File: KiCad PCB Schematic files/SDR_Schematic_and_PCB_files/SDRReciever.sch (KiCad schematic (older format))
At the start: 62 parts, among them J1 Conn_Coaxial, J10 I_0, J11 I_180, J12 Q_90, J13 Q_270, J16 5V, J17 4.3V, J2 AudioJack3, J3 FIL_I, J4 FIL_O, J5 CLK_1, J6 CLK_2, J7 CLK_0, Q1 PN2222A, Q2 BSS138, Q3 BSS138, U1 Si5351A-B-GT, U2 LM4562, U3 SN74CBT3253, Y1 ATS250

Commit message: Removed old KiCad version files, kept the latest and removed *02 appending
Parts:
- removed D1, D2: 1N914, Diode_THT:D_DO-35_SOD27_P7.62mm_Horizontal, symbol SDRReciever-rescue:1N914-Diode
- added J8: 3.3V, Connector_PinHeader_2.54mm:PinHeader_1x01_P2.54mm_Vertical, symbol SDRReciever-rescue:Conn_01x01-Connector_Generic-SDRReciever-rescue
- A1: symbol SDRReciever-rescue:Arduino_Nano_v3.x-MCU_Module -> SDRReciever-rescue:Arduino_Nano_v3.x-MCU_Module-SDRReciever-rescue
- C1, C3: footprint Capacitor_THT:C_Disc_D4.7mm_W2.5mm_P5.00mm -> Capacitor_SMD:C_0805_2012Metric; symbol SDRReciever-rescue:C-Device -> SDRReciever-rescue:C-Device-SDRReciever-rescue
- C10, C11, C12, C13, C4: footprint Capacitor_THT:C_Disc_D5.1mm_W3.2mm_P5.00mm -> Capacitor_SMD:C_0805_2012Metric; symbol SDRReciever-rescue:C-Device -> SDRReciever-rescue:C-Device-SDRReciever-rescue
- C14, C15, C16, C2, C5, C6, C7: footprint Capacitor_THT:C_Disc_D5.0mm_W2.5mm_P2.50mm -> Capacitor_SMD:C_0805_2012Metric; symbol SDRReciever-rescue:C-Device -> SDRReciever-rescue:C-Device-SDRReciever-rescue
- C9: footprint Capacitor_THT:CP_Radial_D5.0mm_P2.00mm -> Capacitor_SMD:C_0805_2012Metric; symbol SDRReciever-rescue:C-Device -> SDRReciever-rescue:C-Device-SDRReciever-rescue
- J1: symbol SDRReciever-rescue:Conn_Coaxial-Connector -> SDRReciever-rescue:Conn_Coaxial-Connector-SDRReciever-rescue
- J10, J11, J12, J13, J16, J17, J5, J6, J7: symbol SDRReciever-rescue:Conn_01x01-Connector_Generic -> SDRReciever-rescue:Conn_01x01-Connector_Generic-SDRReciever-rescue
- J2: symbol SDRReciever-rescue:AudioJack3-Connector -> SDRReciever-rescue:AudioJack3-Connector-SDRReciever-rescue
- J3: value FIL_I -> FIL_IN; symbol SDRReciever-rescue:Conn_01x01-Connector_Generic -> SDRReciever-rescue:Conn_01x01-Connector_Generic-SDRReciever-rescue
- J4: value FIL_O -> FIL_OUT; symbol SDRReciever-rescue:Conn_01x01-Connector_Generic -> SDRReciever-rescue:Conn_01x01-Connector_Generic-SDRReciever-rescue
- JP1, JP2, JP3, JP4: symbol SDRReciever-rescue:Jumper_NC_Small-Device -> SDRReciever-rescue:Jumper_NC_Small-Device-SDRReciever-rescue
- L1: footprint Inductor_THT:L_Toroid_Vertical_L13.0mm_W6.5mm_P5.60mm -> Inductor_THT:L_Toroid_Vertical_L10.0mm_W5.0mm_P5.08mm; symbol SDRReciever-rescue:L-Device -> SDRReciever-rescue:L-Device-SDRReciever-rescue
- L2: footprint Inductor_THT:L_Toroid_Vertical_L10.0mm_W5.0mm_P5.08mm -> Inductor_THT:L_Toroid_Vertical_L13.0mm_W6.5mm_P5.60mm; symbol SDRReciever-rescue:L-Device -> SDRReciever-rescue:L-Device-SDRReciever-rescue
- L3: symbol SDRReciever-rescue:L-Device -> SDRReciever-rescue:L-Device-SDRReciever-rescue
- Q1: symbol SDRReciever-rescue:PN2222A-Transistor_BJT -> SDRReciever-rescue:PN2222A-Transistor_BJT-SDRReciever-rescue
- R1, R10, R11, R12, R13, R14, R18, R19, R3, R4, R5: footprint Resistor_THT:R_Axial_DIN0207_L6.3mm_D2.5mm_P7.62mm_Horizontal -> Resistor_SMD:R_0805_2012Metric; symbol SDRReciever-rescue:R-Device -> SDRReciever-rescue:R-Device-SDRReciever-rescue
- R20, R21, R22, R23: symbol SDRReciever-rescue:R-Device -> SDRReciever-rescue:R-Device-SDRReciever-rescue
- R7, R8: footprint (none) -> Resistor_SMD:R_0805_2012Metric; symbol SDRReciever-rescue:R-Device -> SDRReciever-rescue:R-Device-SDRReciever-rescue
- U1: symbol SDRReciever-rescue:Si5351A-B-GT-Oscillator -> SDRReciever-rescue:Si5351A-B-GT-Oscillator-SDRReciever-rescue
- U2: symbol Amplifier_Operational:LM4562 -> SDRReciever-rescue:LM4562-Amplifier_Operational
- U3: symbol SDRReciever-rescue:SN74CBT3253-Analog_Switch -> SDRReciever-rescue:SN74CBT3253-Analog_Switch-SDRReciever-rescue
- Y1: value ATS250 -> CX3225SB; footprint Crystal:Crystal_HC49-U_Vertical -> Crystal:Crystal_SMD_Abracon_ABM8G-4Pin_3.2x2.5mm; symbol SDRReciever-rescue:Crystal-Device -> Device:Crystal_GND24; DigiKey (none) -> https://www.digikey.com/en/products/detail/kyocera-internat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
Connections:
- wire segments 183 -> 181
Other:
- note added: "CX3225SB\n25 MHz crystal"
- note added: "Full Scale Input \nSignal Level Typ: 1.0 Vrms\nInput R = 55kΩ?????"
- note added: "Optional\nbypass jumper"
- note added: "T37-6 Toroid:\n11.9 turns"
- note added: "T50-6 Toroid: \n14.3 turns"
- note removed: "Full Scale Input \nSignal Level Typ: 1.0 Vrms\nInput R = 55kΩ."
- note removed: "NOTE:\nDouble check values of C5-C8\n100nf?"
- note removed: "Note:\nCheck all footprints\nExchange some through hole components for surface mount"
- note removed: "T37-6 Toroid:\n-- turns"
- note removed: "T50-6 Toroid: \n-- turns"
- note removed: "The ATS250 is \na low-cost 25 \nMHz crystal\n\nCX3225\n25 MHz crystal"
- note removed: "Voltage Protection Diodes:\nThese will prevent too large of signals \nfrom coming through"
- moved on the sheet: Q3

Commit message: Revision 0.3 of schematic Added bypass cap Added DC blocking caps Removed redudant resitors Added custom footprints Updated BNC connector footprint Updated audo jack footprint, schematic symbol, connections, and 3D model Updated comments Removed old PCB Created new blank PCB
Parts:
- removed R7, R8: 1k, Resistor_SMD:R_0805_2012Metric, symbol SDRReciever-rescue:R-Device-SDRReciever-rescue
- added C16: 0.1u, Capacitor_SMD:C_0805_2012Metric, symbol SDRReciever-rescue:C-Device-SDRReciever-rescue
- added C17, C18: 10u, Capacitor_SMD:C_0805_2012Metric, symbol SDRReciever-rescue:C-Device-SDRReciever-rescue
- J1: footprint Connector_Coaxial:SMA_Molex_73251-1153_EdgeMount_Horizontal -> Connector_TE-Connectivity:BNC_Socket_TYCO-AMP_LargePads
- J14: renamed from J2; footprint Connector_Audio:Jack_3.5mm_Switronic_ST-005-G_horizontal -> Connector_Audio:35RAPC4BHN2; symbol SDRReciever-rescue:AudioJack3-Connector-SDRReciever-rescue -> 35RAPC4BHN2:35RAPC4BHN2; Soundcard Datasheet (none) -> https://static.qobuz.com/info/IMG/pdf/VT1620A.pdf
- renumbered C9 to C1, C14 to C10, C15 to C11, C16 to C12, C5 to C13, C6 to C14, C7 to C15, C1 to C3, C3 to C4, C11 to C5, C4 to C6, C10 to C7, C12 to C8, C13 to C9, J8 to J2, J16 to J4, J17 to J5, J4 to J6, J6 to J7, J7 to J8, J5 to J9, JP3 to JP2, JP2 to JP3, L2 to L1, L1 to L2, R20 to R1, R11 to R10, R12 to R11, R4 to R12, R3 to R14, R14 to R15, R1 to R2, R21 to R3, R22 to R4, R23 to R5, R18 to R6, R19 to R7, R5 to R8, R10 to R9, U3 to U2, U2 to U3
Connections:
- net +4.3V: now also C16.1
- net GND: now also C16.2
- net at C14.1, R14.1, U3.7: now also C18.2; no longer J14.R
- net at JP4.2: now also J14.1; no longer J14.S
- net at C11.1, R12.1, U3.1: now also C17.2; no longer J14.T
- new net: C17.1, J14.2
- new net: C18.1, J14.3
- no-connect marks 24 -> 26
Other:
- note added: "DC Blocking\nCapcitor"
- note added: "Full Scale Input \nSignal Level Typ: 1.0 Vrms\nSound Card Input R = 55kΩ"
- note removed: "Full Scale Input \nSignal Level Typ: 1.0 Vrms\nInput R = 55kΩ?????"
- moved on the sheet: JP4

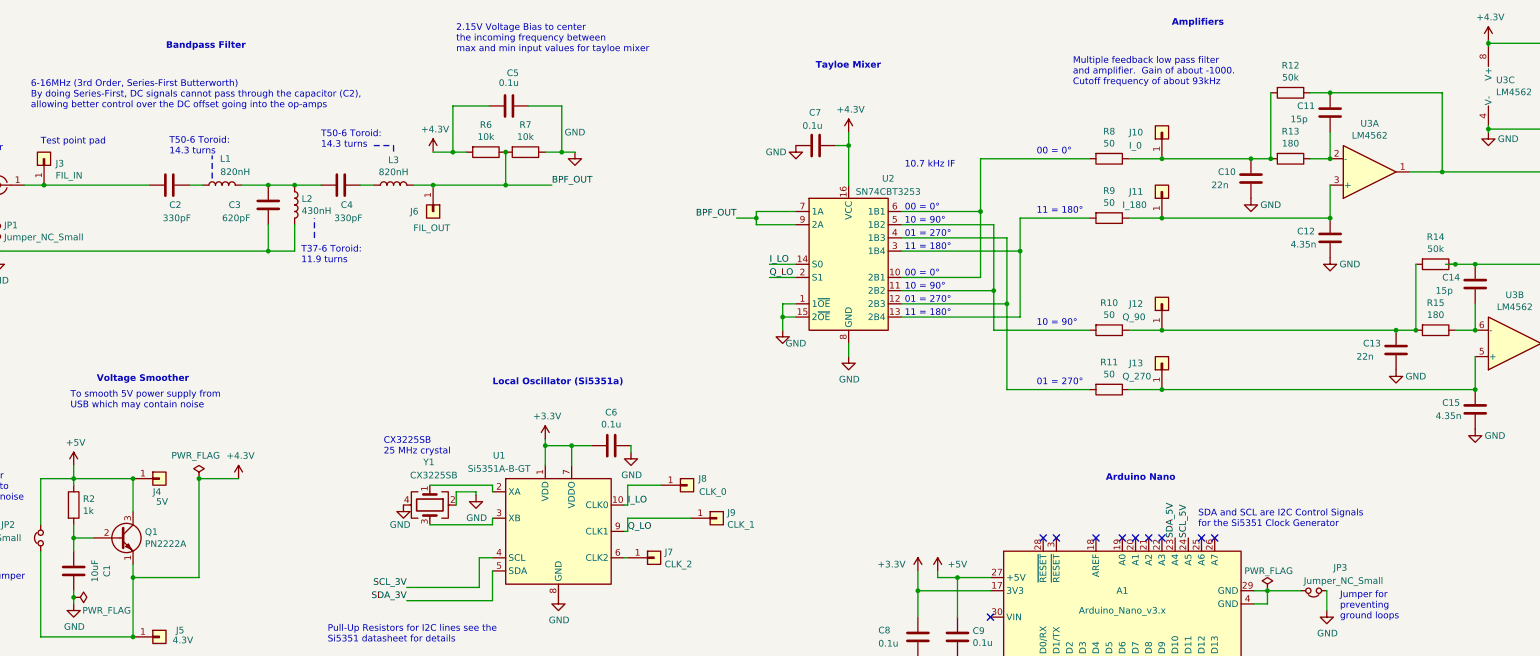
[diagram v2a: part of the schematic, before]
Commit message: Exchanged transistor for surface mount transistor Updated resistor values to standard values
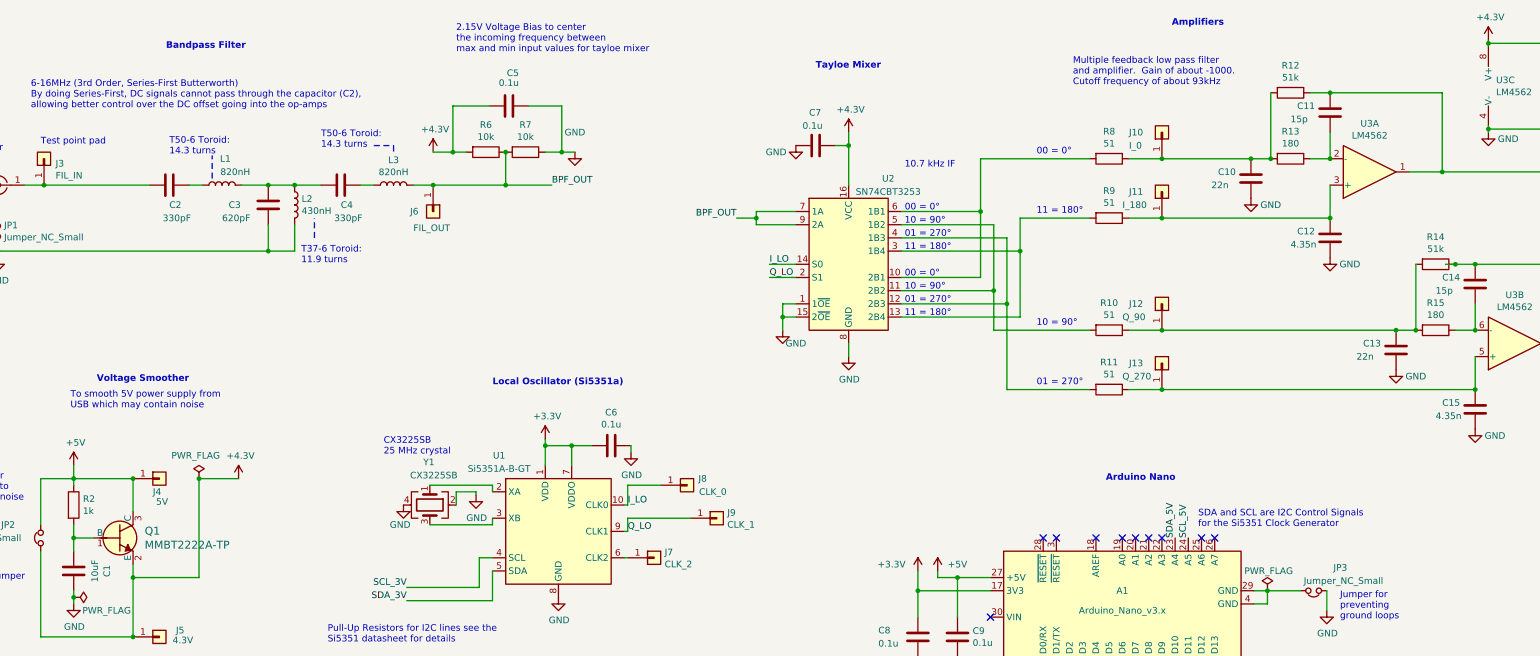
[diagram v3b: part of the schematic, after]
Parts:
- removed Q1: PN2222A, Package_TO_SOT_THT:TO-92_Inline, symbol SDRReciever-rescue:PN2222A-Transistor_BJT-SDRReciever-rescue
- added Q1: MMBT2222A-TP, digikey-footprints:SOT-23-3, symbol dk_Transistors-Bipolar-BJT-Single:MMBT2222A-TP
- R10, R11, R8, R9: value 50 -> 51
- R12, R14: value 50k -> 51k
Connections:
- net +4.3V: now also Q1.2 (E)
- net +5V: now also Q1.3 (C)
- net at C1.2, R2.2: now also Q1.1 (B)
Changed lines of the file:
@@
 P 10425 1700
 F 0 "R8" V 10218 1700 50  0000 C CNN
-F 1 "50" V 10309 1700 50  0000 C CNN
+F 1 "51" V 10309 1700 50  0000 C CNN
 F 2 "Resistor_SMD:R_0805_2012Metric" V 10355 1700 50  0001 C CNN
 F 3 "~" H 10425 1700 50  0001 C CNN
@@
 P 10425 2150
 F 0 "R9" V 10218 2150 50  0000 C CNN
-F 1 "50" V 10309 2150 50  0000 C CNN
+F 1 "51" V 10309 2150 50  0000 C CNN
 F 2 "Resistor_SMD:R_0805_2012Metric" V 10355 2150 50  0001 C CNN
 F 3 "~" H 10425 2150 50  0001 C CNN
@@
 P 10425 3000
 F 0 "R10" V 10218 3000 50  0000 C CNN
-F 1 "50" V 10309 3000 50  0000 C CNN
+F 1 "51" V 10309 3000 50  0000 C CNN
 F 2 "Resistor_SMD:R_0805_2012Metric" V 10355 3000 50  0001 C CNN
 F 3 "~" H 10425 3000 50  0001 C CNN
@@
 P 10425 3450
 F 0 "R11" V 10218 3450 50  0000 C CNN
-F 1 "50" V 10309 3450 50  0000 C CNN
+F 1 "51" V 10309 3450 50  0000 C CNN
 F 2 "Resistor_SMD:R_0805_2012Metric" V 10355 3450 50  0001 C CNN
 F 3 "~" H 10425 3450 50  0001 C CNN
@@
 	1    15000 2950
 	0    -1   -1   0
-$EndComp
-$Comp
-L SDRReciever-rescue:PN2222A-Transistor_BJT-SDRReciever-rescue Q1
-U 1 1 5F391EB1
-P 2925 4575
-F 0 "Q1" H 3115 4621 50  0000 L CNN
-F 1 "PN2222A" H 3115 4530 50  0000 L CNN
-F 2 "Package_TO_SOT_THT:TO-92_Inline" H 3125 4500 50  0001 L CIN
-F 3 "http://www.fairchildsemi.com/ds/PN/PN2222A.pdf" H 2925 4575 50  0001 L CNN
-	1    2925 4575
-	1    0    0    -1
 $EndComp
 Wire Wire Line
@@
 P 11800 1200
 F 0 "R12" V 11593 1200 50  0000 C CNN
-F 1 "50k" V 11684 1200 50  0000 C CNN
+F 1 "51k" V 11684 1200 50  0000 C CNN
 F 2 "Resistor_SMD:R_0805_2012Metric" V 11730 1200 50  0001 C CNN
 F 3 "~" H 11800 1200 50  0001 C CNN
@@
 P 12900 2500
 F 0 "R14" V 12693 2500 50  0000 C CNN
-F 1 "50k" V 12784 2500 50  0000 C CNN
+F 1 "51k" V 12784 2500 50  0000 C CNN
 F 2 "Resistor_SMD:R_0805_2012Metric" V 12830 2500 50  0001 C CNN
 F 3 "~" H 12900 2500 50  0001 C CNN
@@
 NoConn ~ 15000 2550
 NoConn ~ 15000 2650
+$Comp
+L dk_Transistors-Bipolar-BJT-Single:MMBT2222A-TP Q1
+U 1 1 608B107C
+P 2925 4575
+F 0 "Q1" H 3113 4628 60  0000 L CNN
+F 1 "MMBT2222A-TP" H 3113 4522 60  0000 L CNN
+F 2 "digikey-footprints:SOT-23-3" H 3125 4775 60  0001 L CNN
+F 3 "https://www.mccsemi.com/pdf/Products/MMBT2222A(SOT-23).pdf" H 3125 4875 60  0001 L CNN
+F 4 "MMBT2222ATPMSCT-ND" H 3125 4975 60  0001 L CNN "Digi-Key_PN"
+F 5 "MMBT2222A-TP" H 3125 5075 60  0001 L CNN "MPN"
+F 6 "Discrete Semiconductor Products" H 3125 5175 60  0001 L CNN "Category"
+F 7 "Transistors - Bipolar (BJT) - Single" H 3125 5275 60  0001 L CNN "Family"
+F 8 "https://www.mccsemi.com/pdf/Products/MMBT2222A(SOT-23).pdf" H 3125 5375 60  0001 L CNN "DK_Datasheet_Link"
+F 9 "/product-detail/en/micro-commercial-co/MMBT2222A-TP/MMBT2222ATPMSCT-ND/717394" H 3125 5475 60  0001 L CNN "DK_Detail_Page"
+F 10 "TRANS NPN 40V 0.6A SOT23" H 3125 5575 60  0001 L CNN "Description"
+F 11 "Micro Commercial Co" H 3125 5675 60  0001 L CNN "Manufacturer"
+F 12 "Active" H 3125 5775 60  0001 L CNN "Status"
+	1    2925 4575
+	1    0    0    -1
+$EndComp
 $EndSCHEMATC
